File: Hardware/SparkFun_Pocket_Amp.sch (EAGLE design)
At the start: 52 parts, among them J1 AUDIO_JACK, J2 AUDIO_JACK, J3 micro USB, U1 LM4853, U2 LM358, U3 TPS61200, U4 MCP73831

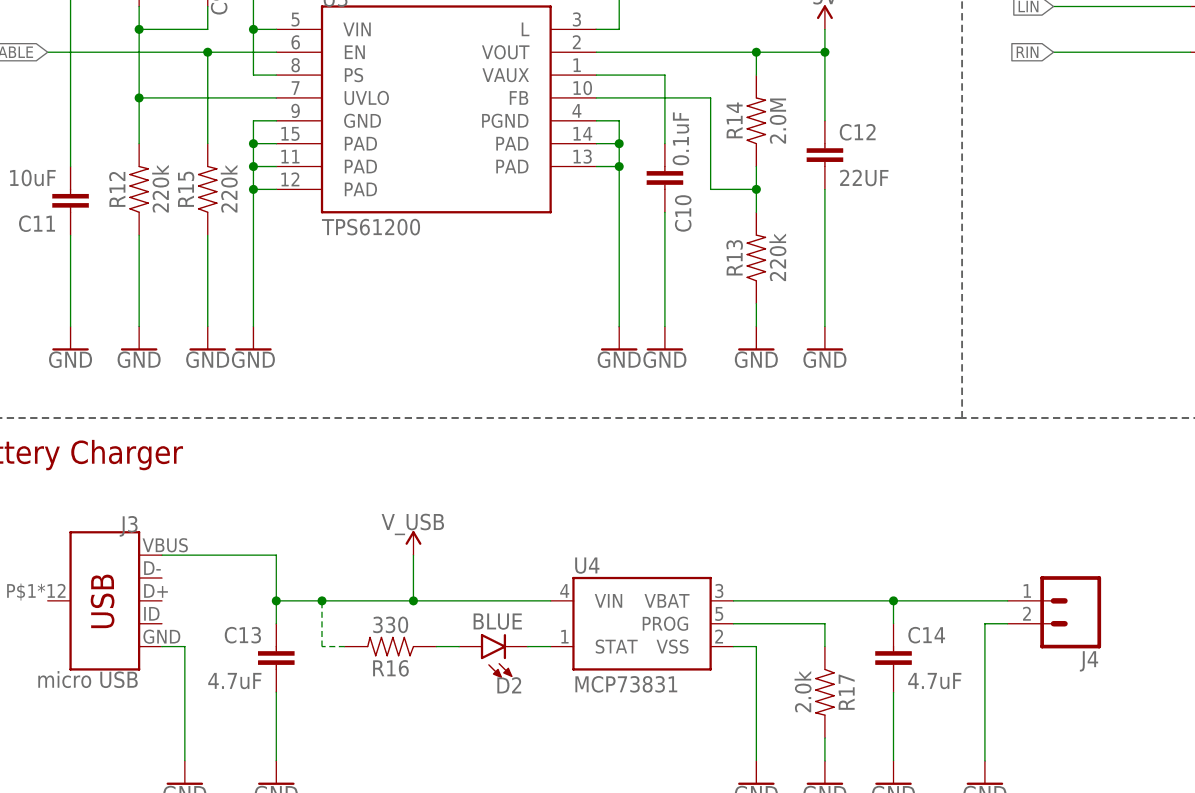
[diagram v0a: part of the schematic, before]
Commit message: Added PROD_ID to C12
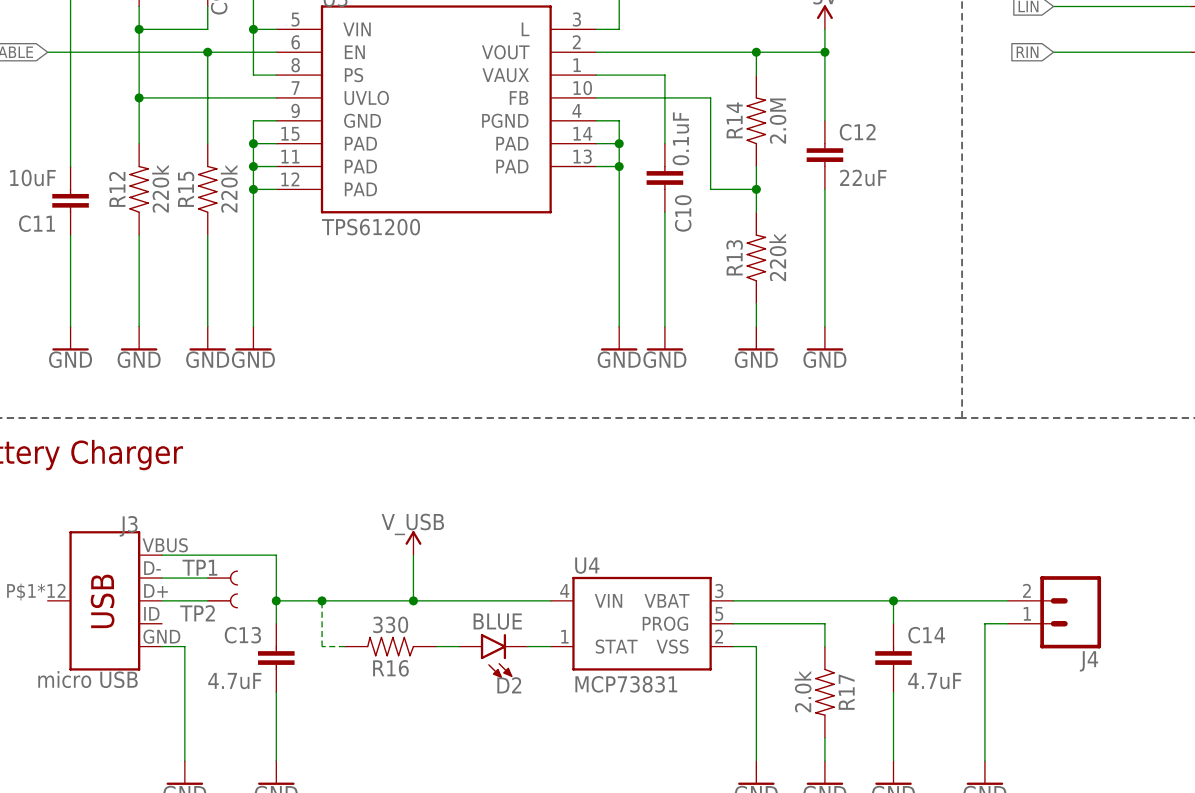
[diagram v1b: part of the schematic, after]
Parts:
- added TP1, TP2: TEST-POINT3, SparkFun-Connectors:TEST-POINT3
- C12: value 22UF -> 22uF
- J4: device SparkFun-Connectors:CONN_02POLAR -> SparkFun-Connectors:CONN_02-JST-2MM-SMT
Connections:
- new net N$10: J3.D-, TP1.1
- new net N$18: J3.D+, TP2.1
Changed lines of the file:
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@@
 <part name="R13" library="SparkFun-Resistors" deviceset="220KOHM" device="-0603-1/10W-1%" value="220k"/>
 <part name="R14" library="SparkFun-Resistors" deviceset="2MOHMS" device="-0603-1/10W-1%" value="2.0M"/>
-<part name="C12" library="SparkFun-Capacitors" deviceset="22UF" device="-1210-16V-20%" value="22UF"/>
+<part name="C12" library="SparkFun-Capacitors" deviceset="22UF" device="-1210-16V-20%" value="22uF"/>
 <part name="GND11" library="SparkFun-PowerSymbols" deviceset="GND" device=""/>
 <part name="GND12" library="SparkFun-PowerSymbols" deviceset="GND" device=""/>
@@
 <part name="C14" library="SparkFun-Capacitors" deviceset="4.7UF" device="0603" value="4.7uF"/>
 <part name="J3" library="SparkFun-Connectors" deviceset="USB_MICRO-B" device="_HALF_PTH" value="micro USB"/>
-<part name="J4" library="SparkFun-Connectors" deviceset="CONN_02" device="POLAR"/>
+<part name="J4" library="SparkFun-Connectors" deviceset="CONN_02" device="-JST-2MM-SMT"/>
 <part name="GND19" library="SparkFun-PowerSymbols" deviceset="GND" device=""/>
 <part name="GND20" library="SparkFun-PowerSymbols" deviceset="GND" device=""/>
@@
 <part name="LOGO2" library="SparkFun-Aesthetics" deviceset="OSHW-LOGO" device="M"/>
 <part name="SUPPLY12" library="SparkFun-PowerSymbols" deviceset="V_USB" device=""/>
+<part name="TP1" library="SparkFun-Connectors" deviceset="TEST-POINT" device="3" value=""/>
+<part name="TP2" library="SparkFun-Connectors" deviceset="TEST-POINT" device="3" value=""/>
 </parts>
 <sheets>
@@
 <instance part="LOGO2" gate="G$1" x="73.66" y="12.7"/>
 <instance part="SUPPLY12" gate="G$1" x="53.34" y="93.98"/>
+<instance part="TP1" gate="G$1" x="30.48" y="91.44" smashed="yes">
+<attribute name="NAME" x="27.686" y="91.694" size="1.778" layer="95" font="vector"/>
+<attribute name="VALUE" x="27.94" y="88.9" size="1.778" layer="96" font="vector"/>
+</instance>
+<instance part="TP2" gate="G$1" x="30.48" y="88.9" smashed="yes">
+<attribute name="NAME" x="27.432" y="86.614" size="1.778" layer="95" font="vector"/>
+<attribute name="VALUE" x="27.94" y="86.36" size="1.778" layer="96" font="vector"/>
+</instance>
 </instances>
 <busses>
@@
 </segment>
 </net>
+<net name="N$10" class="0">
+<segment>
+<pinref part="J3" gate="G$1" pin="D-"/>
+<wire x1="25.4" y1="91.44" x2="30.48" y2="91.44" width="0.1524" layer="91"/>
+<pinref part="TP1" gate="G$1" pin="1"/>
+</segment>
+</net>
+<net name="N$18" class="0">
+<segment>
+<pinref part="J3" gate="G$1" pin="D+"/>
+<wire x1="25.4" y1="88.9" x2="30.48" y2="88.9" width="0.1524" layer="91"/>
+<pinref part="TP2" gate="G$1" pin="1"/>
+</segment>
+</net>

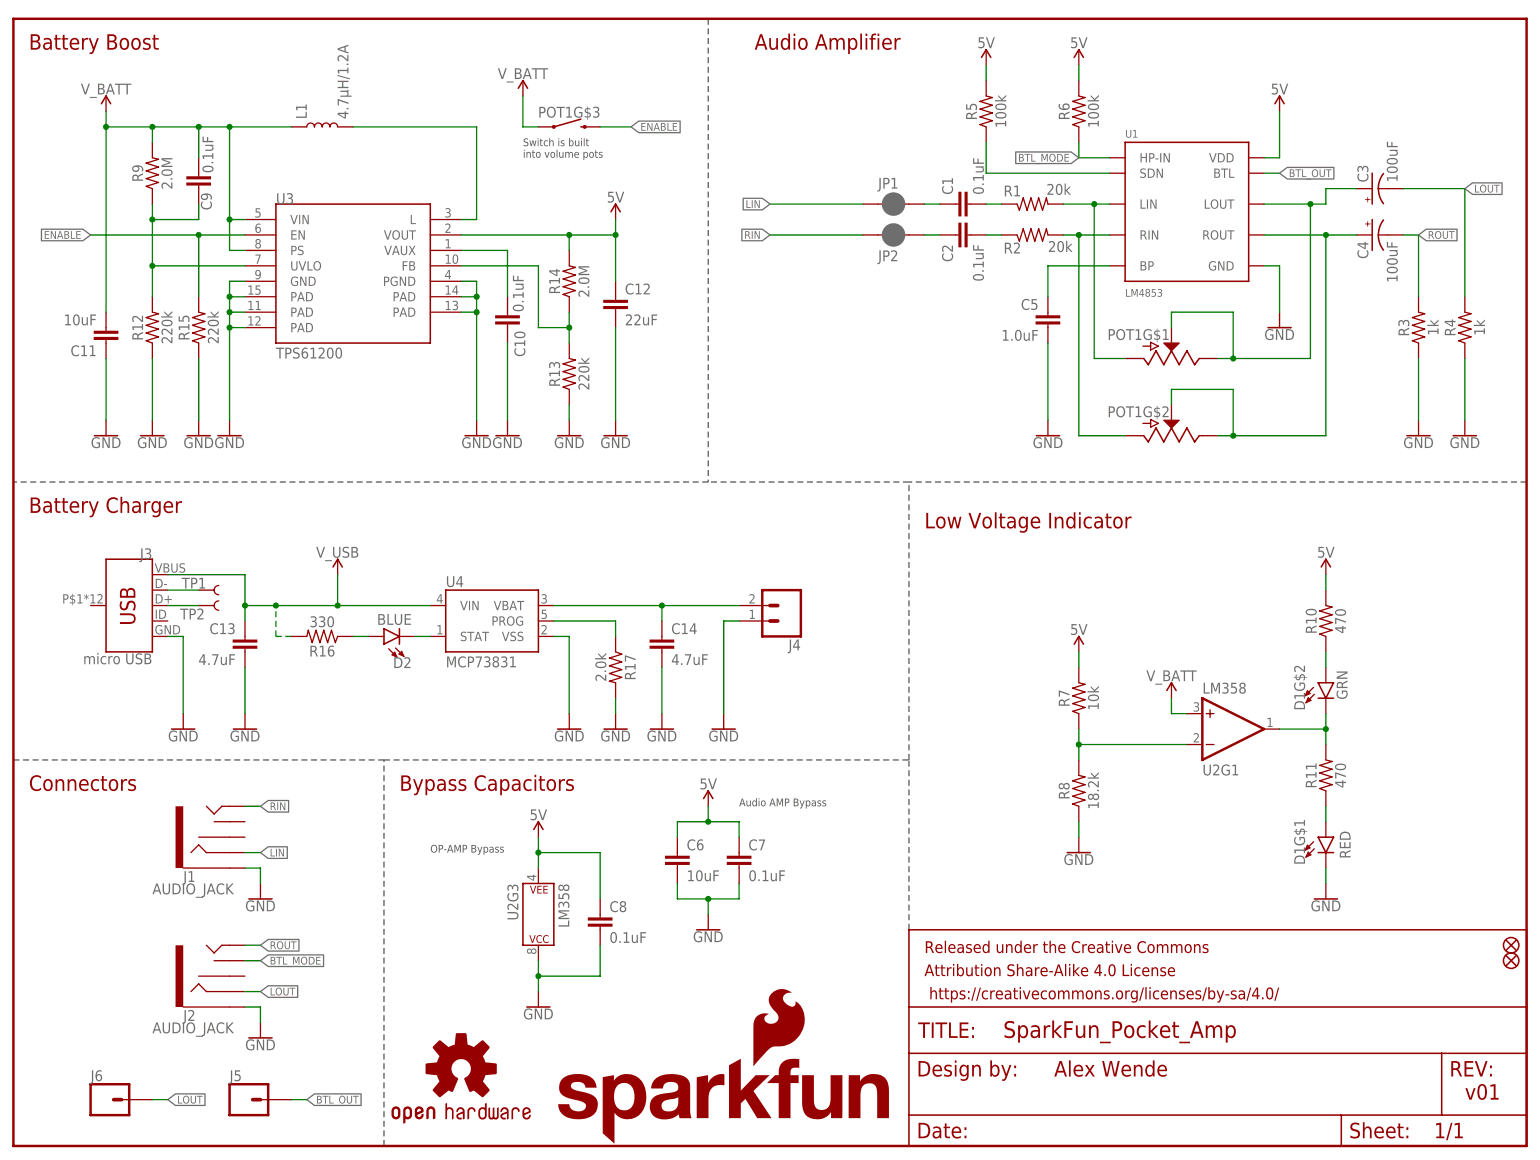
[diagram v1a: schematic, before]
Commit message: DFM Changes
Added values missing on a few parts
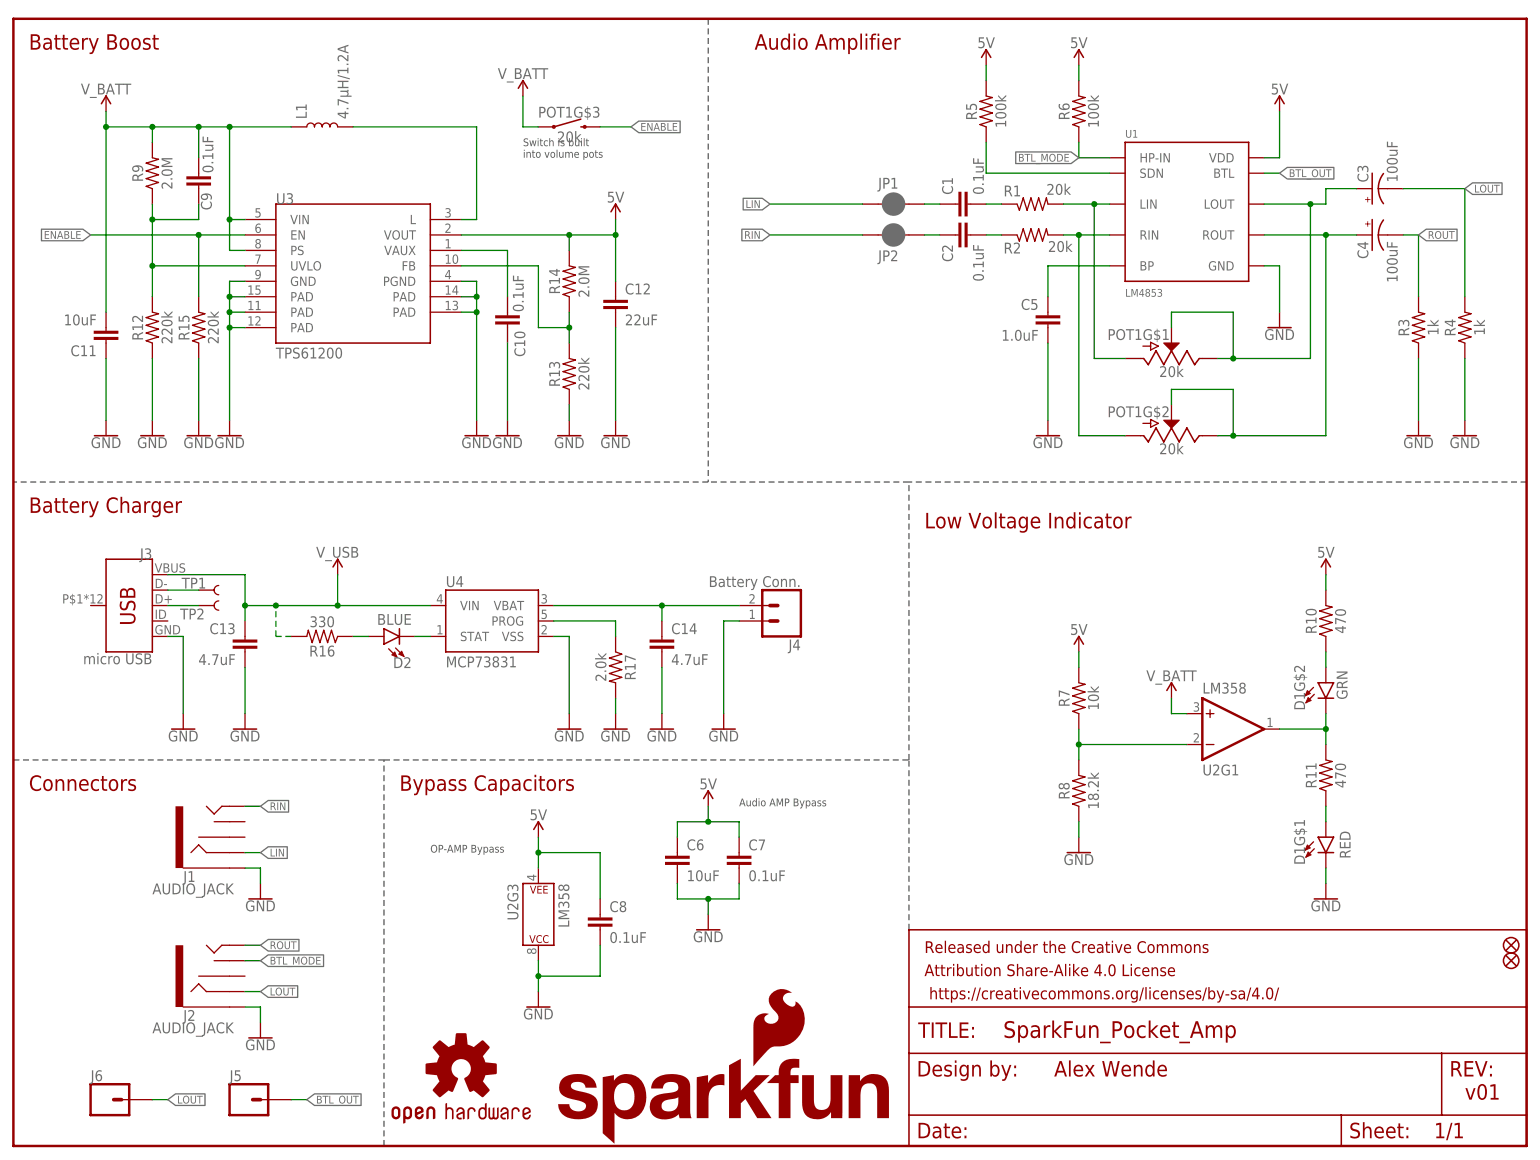
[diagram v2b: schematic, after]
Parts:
- D1: value LED_RG6300T15 -> LED Inicator
- J4: value (none) -> Battery Conn.
- POT1: value POTENTIOMETER_DUAL_W/SWITCH -> 20k
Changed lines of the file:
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@@
 <part name="GND2" library="SparkFun-PowerSymbols" deviceset="GND" device=""/>
 <part name="GND3" library="SparkFun-PowerSymbols" deviceset="GND" device=""/>
-<part name="POT1" library="SparkFun-Resistors" deviceset="POTENTIOMETER_DUAL_W/SWITCH" device="" value=""/>
+<part name="POT1" library="SparkFun-Resistors" deviceset="POTENTIOMETER_DUAL_W/SWITCH" device="" value="20k"/>
 <part name="C5" library="SparkFun-Capacitors" deviceset="1.0UF" device="-0603-16V-10%" value="1.0uF"/>
 <part name="GND4" library="SparkFun-PowerSymbols" deviceset="GND" device=""/>
@@
 <part name="R11" library="SparkFun-Resistors" deviceset="RESISTOR" device="AXIAL-0.3-KIT" value="470"/>
 <part name="GND10" library="SparkFun-PowerSymbols" deviceset="GND" device=""/>
-<part name="D1" library="SparkFun-LED" deviceset="LED_RG" device="6300T15" value=""/>
+<part name="D1" library="SparkFun-LED" deviceset="LED_RG" device="6300T15" value="LED Inicator"/>
 <part name="U2" library="SparkFun-IC-Amplifiers" deviceset="LM358" device="KIT" value="LM358"/>
 <part name="U3" library="SparkFun-IC-Power" deviceset="TPS61200" device=""/>
@@
 <part name="C14" library="SparkFun-Capacitors" deviceset="4.7UF" device="0603" value="4.7uF"/>
 <part name="J3" library="SparkFun-Connectors" deviceset="USB_MICRO-B" device="_HALF_PTH" value="micro USB"/>
-<part name="J4" library="SparkFun-Connectors" deviceset="CONN_02" device="-JST-2MM-SMT"/>
+<part name="J4" library="SparkFun-Connectors" deviceset="CONN_02" device="-JST-2MM-SMT" value="Battery Conn."/>
 <part name="GND19" library="SparkFun-PowerSymbols" deviceset="GND" device=""/>
 <part name="GND20" library="SparkFun-PowerSymbols" deviceset="GND" device=""/>
@@
 <instance part="R11" gate="G$1" x="215.9" y="60.96" rot="R90"/>
 <instance part="GND10" gate="1" x="215.9" y="40.64"/>
-<instance part="D1" gate="G$1" x="215.9" y="50.8"/>
+<instance part="D1" gate="G$1" x="215.9" y="50.8" smashed="yes">
+<attribute name="NAME" x="212.471" y="46.228" size="1.778" layer="95" font="vector" rot="R90"/>
+</instance>
 <instance part="D1" gate="G$2" x="215.9" y="76.2" smashed="yes">
 <attribute name="NAME" x="212.471" y="71.628" size="1.778" layer="95" font="vector" rot="R90"/>
-<attribute name="VALUE" x="217.805" y="71.628" size="1.778" layer="96" font="vector" rot="R90" align="top-left"/>
 </instance>
 <instance part="U2" gate="G1" x="200.66" y="68.58" rot="MR180"/>
